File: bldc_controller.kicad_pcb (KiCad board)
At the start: 4 copper layers, 99.1 x 99.1 mm, 151 parts, among them J1 Conn_01x06_Male, J2 Screw_Terminal_01x04, Q1 2N7002E, Q10 IRLB8721PBF, Q11 IRLB8721PBF, Q2 DMN65D8L-7, Q3 DMN65D8L-7, Q4 MMBT3904, Q5 IRF4905, Q6 IRLB8721PBF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

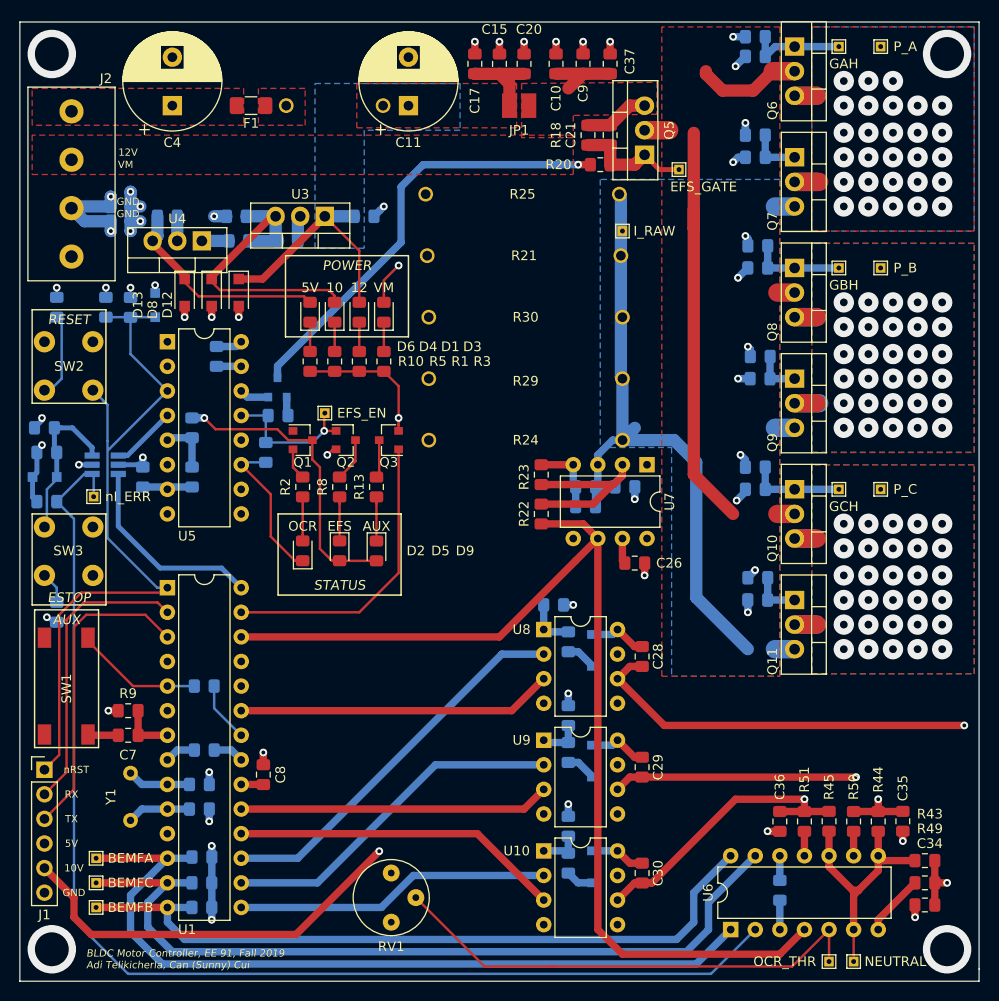
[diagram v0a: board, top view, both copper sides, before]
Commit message: Need to check if output vias are plated
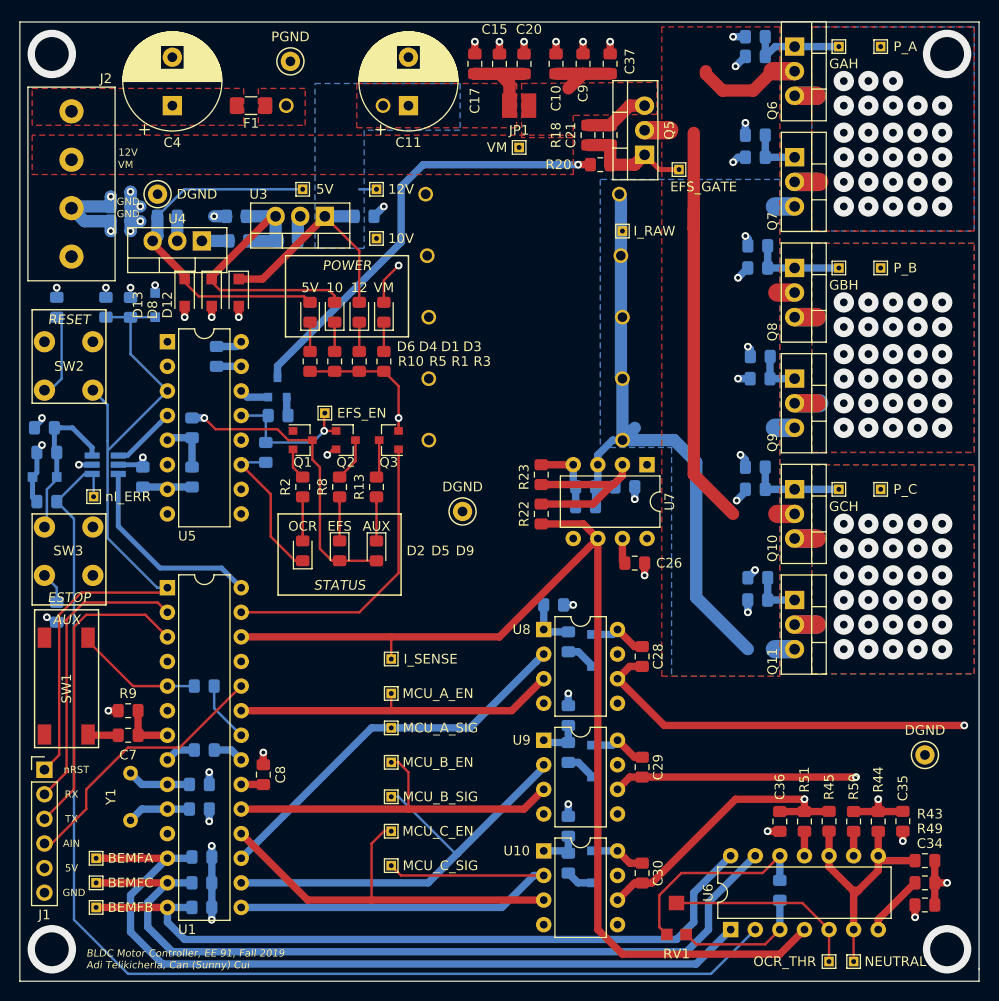
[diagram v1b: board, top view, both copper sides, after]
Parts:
- added TP12: TestPoint, TestPoint:TestPoint_Keystone_5000-5004_Miniature, F.Cu at (146.1, 92.5)
- added TP17: TestPoint, TestPoint:TestPoint_Keystone_5000-5004_Miniature, F.Cu at (193.8, 117.6)
- added TP18: TestPoint, TestPoint:TestPoint_Keystone_5000-5004_Miniature, F.Cu at (128.3, 46.0)
- added TP19: TestPoint, TestPoint:TestPoint_THTPad_1.0x1.0mm_Drill0.5mm, F.Cu at (138.7, 111.3)
- added TP20: TestPoint, TestPoint:TestPoint_THTPad_1.0x1.0mm_Drill0.5mm, F.Cu at (138.7, 129.0)
- added TP21: TestPoint, TestPoint:TestPoint_THTPad_1.0x1.0mm_Drill0.5mm, F.Cu at (138.7, 121.9)
- added TP22: TestPoint, TestPoint:TestPoint_THTPad_1.0x1.0mm_Drill0.5mm, F.Cu at (138.7, 114.8)
- added TP23: TestPoint, TestPoint:TestPoint_THTPad_1.0x1.0mm_Drill0.5mm, F.Cu at (138.7, 125.5)
- added TP24: TestPoint, TestPoint:TestPoint_THTPad_1.0x1.0mm_Drill0.5mm, F.Cu at (138.7, 118.4)
- added TP25: TestPoint, TestPoint:TestPoint_THTPad_1.0x1.0mm_Drill0.5mm, F.Cu at (137.2, 59.2)
- added TP26: TestPoint, TestPoint:TestPoint_THTPad_1.0x1.0mm_Drill0.5mm, F.Cu at (137.2, 64.3)
- added TP27: TestPoint, TestPoint:TestPoint_THTPad_1.0x1.0mm_Drill0.5mm, F.Cu at (129.5, 59.2)
- added TP28: TestPoint, TestPoint:TestPoint_THTPad_1.0x1.0mm_Drill0.5mm, F.Cu at (151.9, 54.9)
- added TP29: TestPoint, TestPoint:TestPoint_Keystone_5000-5004_Miniature, F.Cu at (114.6, 59.7)
- added TP30: TestPoint, TestPoint:TestPoint_THTPad_1.0x1.0mm_Drill0.5mm, F.Cu at (138.7, 107.7)
- R21, R24, R25, R29, R30: moved to B.Cu
- RV1: value 100K -> 5K; footprint Potentiometer_THT:Potentiometer_Bourns_3339P_Vertical_HandSoldering -> Potentiometer_SMD:Trimmer_Pot_SM
- moved RV1 30.1 mm to (168.1, 136.1), turned to 0 degrees
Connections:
- J1 pad 4: +5V -> /ANALOG_IN
- J1 pad 5: +10V -> +5V
- U1 pad 24: Net-(U1-Pad24) -> /ANALOG_IN
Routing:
- net +10V: track 88.6 -> 50.8 mm, vias 1 -> 0
- net Net-(RV1-Pad2): track 50.8 -> 20.2 mm
- net /ANALOG_IN: track 0.00 -> 28.2 mm
- net +5V: track 91.8 -> 118.7 mm
- net GNDD: track 107.6 -> 126.1 mm
- net /MCU_C_SIG: track 32.6 -> 48.8 mm
- net /MCU_B_SIG: track 36.3 -> 45.7 mm
- net /MCU_C_EN: track 34.1 -> 42.5 mm
- net /MCU_B_EN: track 32.6 -> 38.6 mm
- net /I_SENSE: track 111.6 -> 113.9 mm
- net /MCU_A_EN: track 32.6 -> 34.5 mm
- net +12V: track 33.8 -> 35.6 mm
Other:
- board text added: "AIN"
- board text added: "DGND"
- board text added: "I_SENSE"
- board text added: "MCU_A_EN"
- board text added: "MCU_A_SIG"
- board text added: "MCU_B_EN"
- board text added: "MCU_B_SIG"
- board text added: "MCU_C_EN"
- board text added: "MCU_C_SIG"
- board text added: "PGND"

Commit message: Ready for Fab Actually
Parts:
- added REF**: TestPoint_Plated_Hole_D2.0mm, TestPoint:TestPoint_Plated_Hole_D2.0mm, F.Cu at (195.1, 93.7)
- added REF**: TestPoint_Plated_Hole_D2.0mm, TestPoint:TestPoint_Plated_Hole_D2.0mm, F.Cu at (195.1, 78.2)
- added REF**: TestPoint_Plated_Hole_D2.0mm, TestPoint:TestPoint_Plated_Hole_D2.0mm, F.Cu at (195.1, 74.7)
- added REF**: TestPoint_Plated_Hole_D2.0mm, TestPoint:TestPoint_Plated_Hole_D2.0mm, F.Cu at (191.0, 70.9)
- added REF**: TestPoint_Plated_Hole_D2.0mm, TestPoint:TestPoint_Plated_Hole_D2.0mm, F.Cu at (191.0, 54.6)
- added REF**: TestPoint_Plated_Hole_D2.0mm, TestPoint:TestPoint_Plated_Hole_D2.0mm, F.Cu at (191.0, 58.2)
- added REF**: TestPoint_Plated_Hole_D2.0mm, TestPoint:TestPoint_Plated_Hole_D2.0mm, F.Cu at (195.1, 58.2)
- added REF**: TestPoint_Plated_Hole_D2.0mm, TestPoint:TestPoint_Plated_Hole_D2.0mm, F.Cu at (195.1, 54.6)
- added REF**: TestPoint_Plated_Hole_D2.0mm, TestPoint:TestPoint_Plated_Hole_D2.0mm, F.Cu at (191.0, 50.8)
- added REF**: TestPoint_Plated_Hole_D2.0mm, TestPoint:TestPoint_Plated_Hole_D2.0mm, F.Cu at (195.1, 50.8)
- added REF**: TestPoint_Plated_Hole_D2.0mm, TestPoint:TestPoint_Plated_Hole_D2.0mm, F.Cu at (191.0, 97.5)
- added REF**: TestPoint_Plated_Hole_D2.0mm, TestPoint:TestPoint_Plated_Hole_D2.0mm, F.Cu at (191.0, 93.7)
- added REF**: TestPoint_Plated_Hole_D2.0mm, TestPoint:TestPoint_Plated_Hole_D2.0mm, F.Cu at (195.1, 101.1)
- added REF**: TestPoint_Plated_Hole_D2.0mm, TestPoint:TestPoint_Plated_Hole_D2.0mm, F.Cu at (191.0, 101.1)
- added REF**: TestPoint_Plated_Hole_D2.0mm, TestPoint:TestPoint_Plated_Hole_D2.0mm, F.Cu at (195.1, 97.5)
- added REF**: TestPoint_Plated_Hole_D2.0mm, TestPoint:TestPoint_Plated_Hole_D2.0mm, F.Cu at (195.1, 70.9)
- added REF**: TestPoint_Plated_Hole_D2.0mm, TestPoint:TestPoint_Plated_Hole_D2.0mm, F.Cu at (191.0, 74.7)
- added REF**: TestPoint_Plated_Hole_D2.0mm, TestPoint:TestPoint_Plated_Hole_D2.0mm, F.Cu at (191.0, 78.2)
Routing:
- net PhaseC: vias 31 -> 19
- net PhaseB: vias 32 -> 20
- net PhaseA: vias 30 -> 18

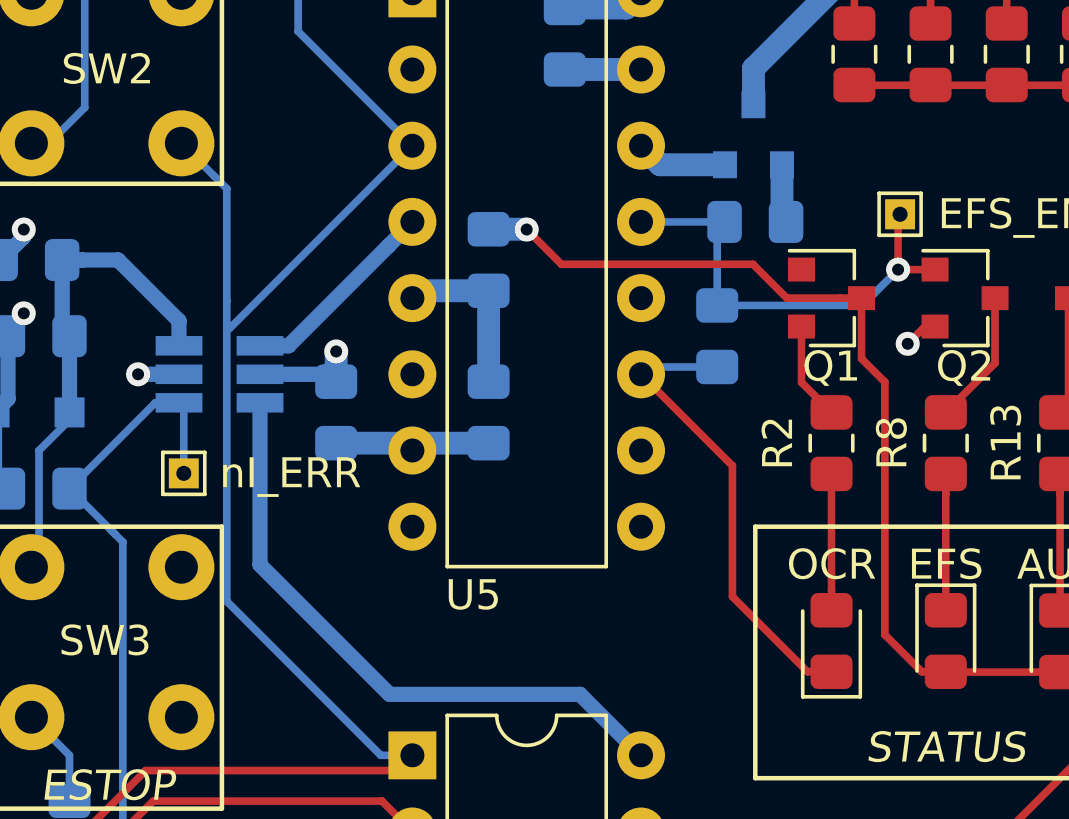
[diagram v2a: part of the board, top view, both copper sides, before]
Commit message: Fixed PMOS footprint
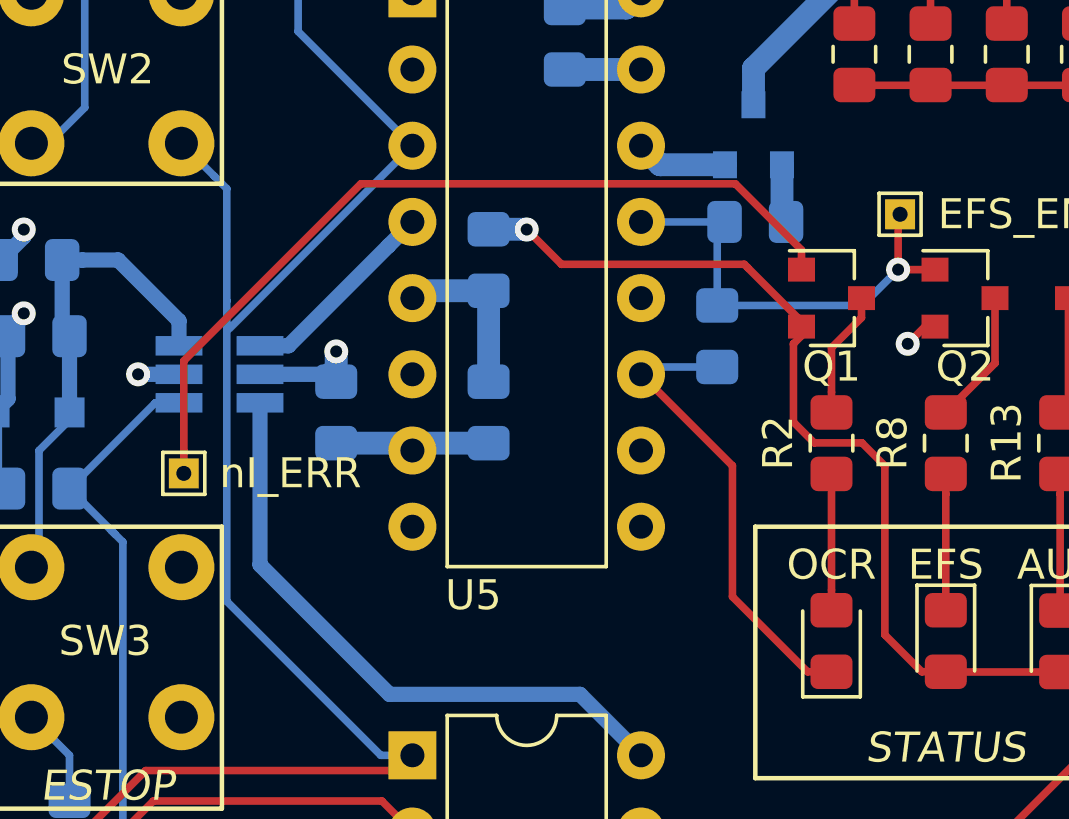
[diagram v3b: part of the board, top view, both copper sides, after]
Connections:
- Q1 pad 1: /nI_ERROR -> /nI_ERR
- Q1 pad 2: Net-(Q1-Pad2) -> +5V
- Q1 pad 3: +5V -> Net-(Q1-Pad3)
- R2 pad 1: Net-(Q1-Pad2) -> Net-(Q1-Pad3)
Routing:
- net /nI_ERR: track 125.9 -> 154.3 mm
- net Net-(Q1-Pad3): track 0.00 -> 4.22 mm
- net Net-(Q1-Pad2): track 3.27 -> 0.00 mm
